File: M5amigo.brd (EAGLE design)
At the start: 50 x 50 mm, 2 parts, among them CN1 CON_PINHD-2X15, CN2 CON_PINHD-2X15

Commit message: better Pinout understanding !
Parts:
- CN1: value CON_PINHD-2X15 -> CON_PINHD-2X15_BOTTOM
- CN2: value CON_PINHD-2X15 -> CON_PINHD-2X15_TOP
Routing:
- net N$19: vias 2 -> 12

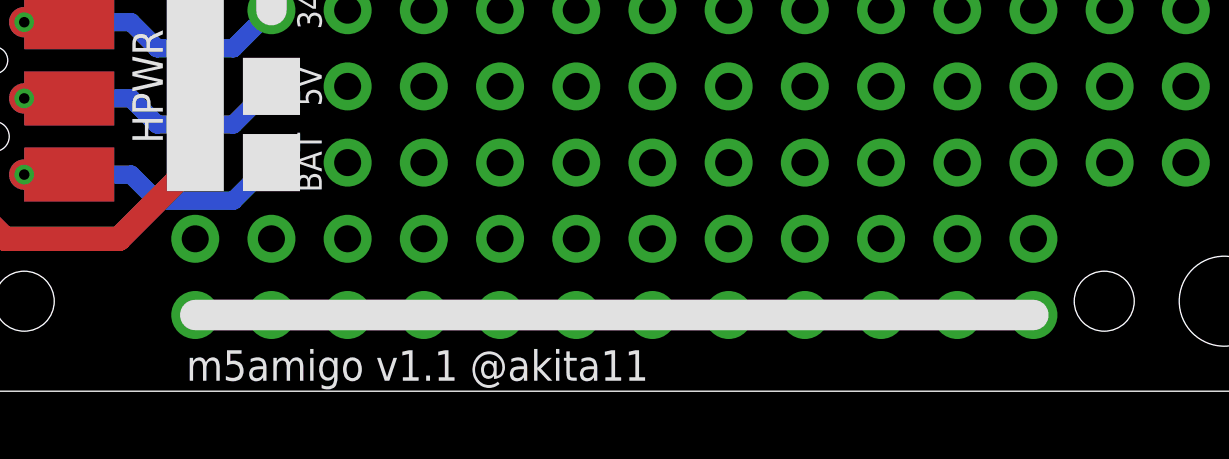
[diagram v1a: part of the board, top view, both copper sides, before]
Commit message: done. now it is more clear, the Pin-Cross is in the Symbol.
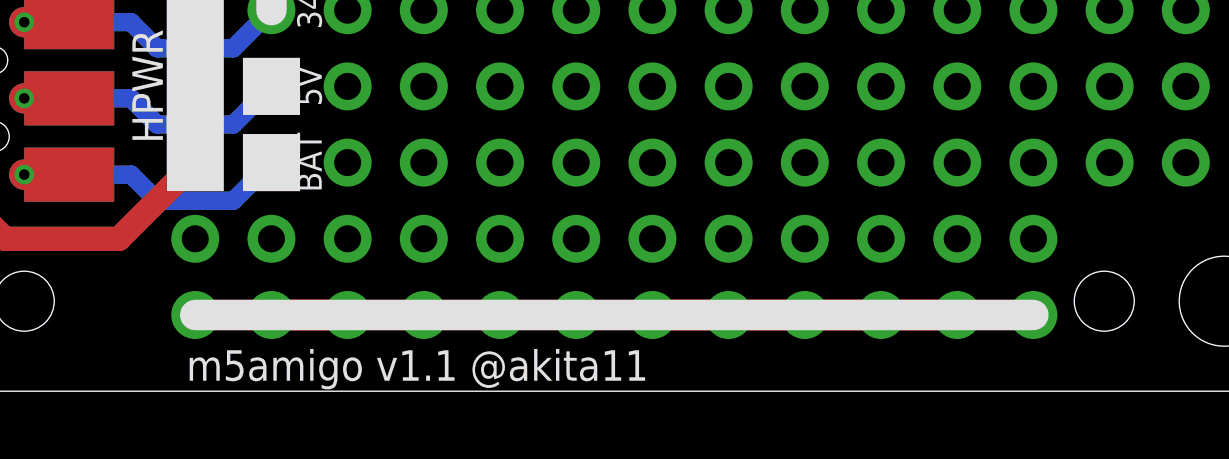
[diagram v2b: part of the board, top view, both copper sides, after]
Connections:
- net 1 renamed G35
- net 10 renamed G19
- net 11 renamed 3.3V
- net 12 renamed G18
- net 13 renamed G1
- net 14 renamed G3
- net 15 renamed G17
- net 16 renamed G16
- net 17 renamed G22
- net 18 renamed G21
- net 19 renamed G5
- net 20 renamed G2
- net 21 renamed G13
- net 22 renamed G12
- net 23 renamed G0
- net 24 renamed G15
- net 25 renamed G34
- net 27 renamed 5V
- net 29 renamed BAT
- net 3 renamed G36
- net 30 renamed HPWR
- net 5 renamed EN
- net 6 renamed GND
- net 7 renamed G25
- net 8 renamed G23
- net 9 renamed G26
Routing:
- net N$19: track 55.9 -> 43.2 mm
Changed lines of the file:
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@@
 </elements>
 <signals>
-<signal name="1">
+<signal name="G35">
 <contactref element="CN2" pad="P$2"/>
 <wire x1="8.5" y1="42.78" x2="7" y2="42.78" width="1.016" layer="16"/>
@@
 <contactref element="CN1" pad="P$1"/>
 </signal>
-<signal name="3">
+<signal name="G36">
 <contactref element="CN2" pad="P$4"/>
 <wire x1="8.5" y1="40.24" x2="7" y2="40.24" width="1.016" layer="1"/>
@@
 <contactref element="CN1" pad="P$3"/>
 </signal>
-<signal name="5">
+<signal name="EN">
 <contactref element="CN2" pad="P$6"/>
 <wire x1="8.5" y1="37.7" x2="7" y2="37.7" width="1.016" layer="16"/>
@@
 <contactref element="CN1" pad="P$5"/>
 </signal>
-<signal name="7">
+<signal name="G25">
 <contactref element="CN2" pad="P$8"/>
 <wire x1="8.5" y1="35.16" x2="7" y2="35.16" width="1.016" layer="1"/>
@@
 <contactref element="CN1" pad="P$7"/>
 </signal>
-<signal name="9">
+<signal name="G26">
 <contactref element="CN2" pad="P$10"/>
 <wire x1="8.5" y1="32.62" x2="7" y2="32.62" width="1.016" layer="16"/>
@@
 <contactref element="CN1" pad="P$9"/>
 </signal>
-<signal name="11">
+<signal name="3.3V">
 <contactref element="CN2" pad="P$12"/>
 <wire x1="8.5" y1="30.08" x2="7" y2="30.08" width="1.016" layer="1"/>
@@
 <contactref element="CN1" pad="P$11"/>
 </signal>
-<signal name="13">
+<signal name="G1">
 <contactref element="CN2" pad="P$14"/>
 <wire x1="8.5" y1="27.54" x2="7" y2="27.54" width="1.016" layer="16"/>
@@
 <contactref element="CN1" pad="P$13"/>
 </signal>
-<signal name="15">
+<signal name="G17">
 <contactref element="CN2" pad="P$16"/>
 <wire x1="8.5" y1="25" x2="7" y2="25" width="1.016" layer="1"/>
@@
 <contactref element="CN1" pad="P$15"/>
 </signal>
-<signal name="17">
+<signal name="G22">
 <contactref element="CN2" pad="P$18"/>
 <wire x1="8.5" y1="22.46" x2="8.89" y2="22.46" width="1.016" layer="16"/>
@@
 <contactref element="CN1" pad="P$17"/>
 </signal>
-<signal name="19">
+<signal name="G5">
 <contactref element="CN2" pad="P$20"/>
 <wire x1="8.5" y1="19.92" x2="7" y2="19.92" width="1.016" layer="1"/>
@@
 <contactref element="CN1" pad="P$19"/>
 </signal>
-<signal name="21">
+<signal name="G13">
 <contactref element="CN2" pad="P$22"/>
 <wire x1="8.5" y1="17.38" x2="7" y2="17.38" width="1.016" layer="16"/>
@@
 <contactref element="CN1" pad="P$21"/>
 </signal>
-<signal name="23">
+<signal name="G0">
 <contactref element="CN2" pad="P$24"/>
 <wire x1="8.5" y1="14.84" x2="7" y2="14.84" width="1.016" layer="1"/>
@@
 <contactref element="CN1" pad="P$23"/>
 </signal>
-<signal name="25">
+<signal name="G34">
 <contactref element="CN2" pad="P$26"/>
 <wire x1="8.5" y1="12.3" x2="7" y2="12.3" width="1.016" layer="16"/>
@@
 <contactref element="CN1" pad="P$25"/>
 </signal>
-<signal name="27">
+<signal name="5V">
 <contactref element="CN2" pad="P$28"/>
 <wire x1="8.5" y1="9.76" x2="7" y2="9.76" width="1.016" layer="1"/>
@@
 <contactref element="CN1" pad="P$27"/>
 </signal>
-<signal name="29">
+<signal name="BAT">
 <contactref element="CN2" pad="P$30"/>
 <wire x1="8.5" y1="7.22" x2="7" y2="7.22" width="1.016" layer="16"/>
@@
 <contactref element="CN1" pad="P$29"/>
 </signal>
-<signal name="6">
+<signal name="GND">
 <contactref element="CN2" pad="P$5"/>
 <wire x1="3.5" y1="37.7" x2="5" y2="37.7" width="1.016" layer="1"/>
@@
 <contactref element="CN1" pad="P$6"/>
 </signal>
-<signal name="8">
+<signal name="G23">
 <contactref element="CN2" pad="P$7"/>
 <wire x1="3.5" y1="35.16" x2="5" y2="35.16" width="1.016" layer="16"/>
@@
 <contactref element="CN1" pad="P$8"/>
 </signal>
-<signal name="10">
+<signal name="G19">
 <contactref element="CN2" pad="P$9"/>
 <wire x1="3.5" y1="32.62" x2="5" y2="32.62" width="1.016" layer="1"/>
@@
 <contactref element="CN1" pad="P$10"/>
 </signal>
-<signal name="12">
+<signal name="G18">
 <contactref element="CN2" pad="P$11"/>
 <wire x1="3.5" y1="30.08" x2="5" y2="30.08" width="1.016" layer="16"/>
@@
 <contactref element="CN1" pad="P$12"/>
 </signal>
-<signal name="14">
+<signal name="G3">
 <contactref element="CN2" pad="P$13"/>
 <wire x1="3.5" y1="27.54" x2="5" y2="27.54" width="1.016" layer="1"/>
@@
 <contactref element="CN1" pad="P$14"/>
 </signal>
-<signal name="16">
+<signal name="G16">
 <contactref element="CN2" pad="P$15"/>
 <wire x1="3.5" y1="25" x2="5" y2="25" width="1.016" layer="16"/>
@@
 <contactref element="CN1" pad="P$16"/>
 </signal>
-<signal name="18">
+<signal name="G21">
 <contactref element="CN2" pad="P$17"/>
 <wire x1="3.5" y1="22.46" x2="5" y2="22.46" width="1.016" layer="1"/>
@@
 <contactref element="CN1" pad="P$18"/>
 </signal>
-<signal name="20">
+<signal name="G2">
 <contactref element="CN2" pad="P$19"/>
 <wire x1="3.5" y1="19.92" x2="5" y2="19.92" width="1.016" layer="16"/>
@@
 <contactref element="CN1" pad="P$20"/>
 </signal>
-<signal name="22">
+<signal name="G12">
 <contactref element="CN2" pad="P$21"/>
 <wire x1="3.5" y1="17.38" x2="5" y2="17.38" width="1.016" layer="1"/>
@@
 <contactref element="CN1" pad="P$22"/>
 </signal>
-<signal name="24">
+<signal name="G15">
 <contactref element="CN2" pad="P$23"/>
 <wire x1="3.5" y1="14.84" x2="5" y2="14.84" width="1.016" layer="16"/>
@@
 <contactref element="CN1" pad="P$24"/>
 </signal>
-<signal name="30">
+<signal name="HPWR">
 <contactref element="CN2" pad="P$29"/>
 <wire x1="3.5" y1="7.22" x2="5" y2="7.22" width="1.016" layer="1"/>
@@
 <via x="12.7" y="2.54" extent="1-16" drill="0.9" diameter="1.6" alwaysstop="yes"/>
 <via x="40.64" y="2.54" extent="1-16" drill="0.9" diameter="1.6" alwaysstop="yes"/>
-<wire x1="12.7" y1="2.54" x2="40.64" y2="2.54" width="1.016" layer="1"/>
-<wire x1="40.64" y1="2.54" x2="12.7" y2="2.54" width="1.016" layer="16"/>
+<wire x1="30.48" y1="2.54" x2="33.02" y2="2.54" width="1.016" layer="1"/>
+<wire x1="33.02" y1="2.54" x2="38.1" y2="2.54" width="1.016" layer="1"/>
 <via x="15.24" y="2.54" extent="1-16" drill="0.9" diameter="1.6" alwaysstop="yes"/>
 <via x="17.78" y="2.54" extent="1-16" drill="0.9" diameter="1.6" alwaysstop="yes"/>
@@
 <via x="27.94" y="2.54" extent="1-16" drill="0.9" diameter="1.6" alwaysstop="yes"/>
 <via x="25.4" y="2.54" extent="1-16" drill="0.9" diameter="1.6" alwaysstop="yes"/>
-<wire x1="35.56" y1="2.54" x2="38.1" y2="2.54" width="0" layer="19" extent="1-1"/>
-<wire x1="33.02" y1="2.54" x2="35.56" y2="2.54" width="0" layer="19" extent="1-1"/>
-<wire x1="30.48" y1="2.54" x2="33.02" y2="2.54" width="0" layer="19" extent="1-1"/>
-<wire x1="27.94" y1="2.54" x2="30.48" y2="2.54" width="0" layer="19" extent="1-1"/>
-<wire x1="25.4" y1="2.54" x2="27.94" y2="2.54" width="0" layer="19" extent="1-1"/>
-<wire x1="22.86" y1="2.54" x2="25.4" y2="2.54" width="0" layer="19" extent="1-1"/>
-<wire x1="20.32" y1="2.54" x2="22.86" y2="2.54" width="0" layer="19" extent="1-1"/>
-<wire x1="17.78" y1="2.54" x2="20.32" y2="2.54" width="0" layer="19" extent="1-1"/>
-<wire x1="15.24" y1="2.54" x2="17.78" y2="2.54" width="0" layer="19" extent="1-1"/>
-<wire x1="40.64" y1="2.54" x2="38.1" y2="2.54" width="0" layer="19" extent="1-1"/>
+<wire x1="12.7" y1="2.54" x2="17.78" y2="2.54" width="1.016" layer="1"/>
+<wire x1="25.4" y1="2.54" x2="30.48" y2="2.54" width="1.016" layer="1"/>
+<wire x1="30.48" y1="2.54" x2="38.1" y2="2.54" width="1.016" layer="1"/>
+<wire x1="38.1" y1="2.54" x2="40.64" y2="2.54" width="1.016" layer="1"/>
+<wire x1="22.86" y1="2.54" x2="25.4" y2="2.54" width="1.016" layer="1"/>
+<wire x1="20.32" y1="2.54" x2="22.86" y2="2.54" width="1.016" layer="1"/>
+<wire x1="17.78" y1="2.54" x2="20.32" y2="2.54" width="1.016" layer="1"/>
+<wire x1="35.56" y1="2.54" x2="38.1" y2="2.54" width="1.016" layer="1"/>
+<wire x1="27.94" y1="2.54" x2="30.48" y2="2.54" width="1.016" layer="1"/>
+<wire x1="15.24" y1="2.54" x2="17.78" y2="2.54" width="1.016" layer="1"/>
 </signal>
 <signal name="N$21">
